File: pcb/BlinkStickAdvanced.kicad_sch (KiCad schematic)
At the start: 27 parts, among them J1 POWER, J2 USB_B_Micro, J3 ADD_HEADER_B, J4 ADD_HEADER_G, J5 ADD_HEADER_R, J6 RGB_HEADER, J7 RGB_HEADER, Q1 IRLR8726, Q2 IRLR8726, Q3 IRLR8726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

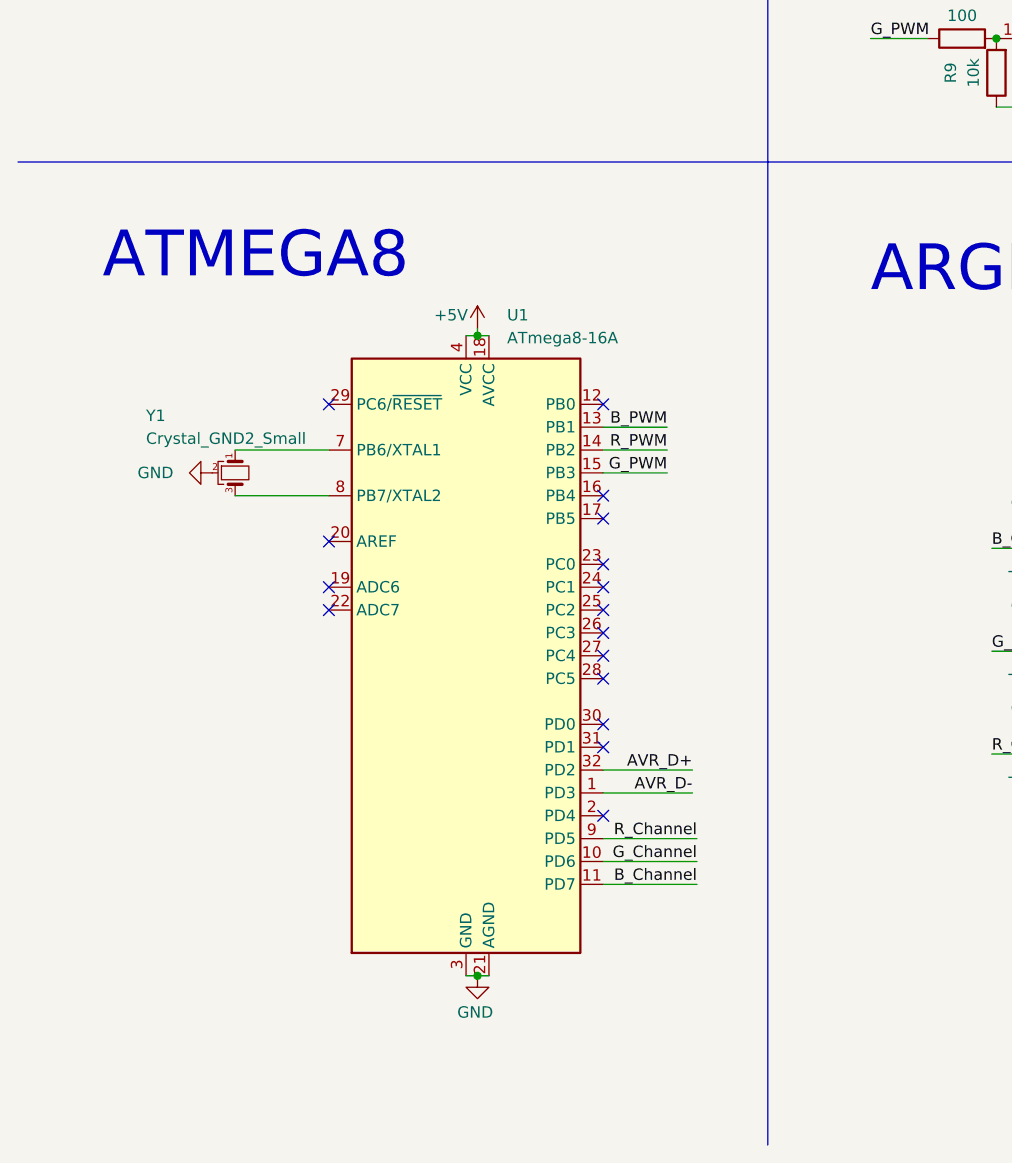
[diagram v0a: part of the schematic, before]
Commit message: USBaspLoader support for PCB.
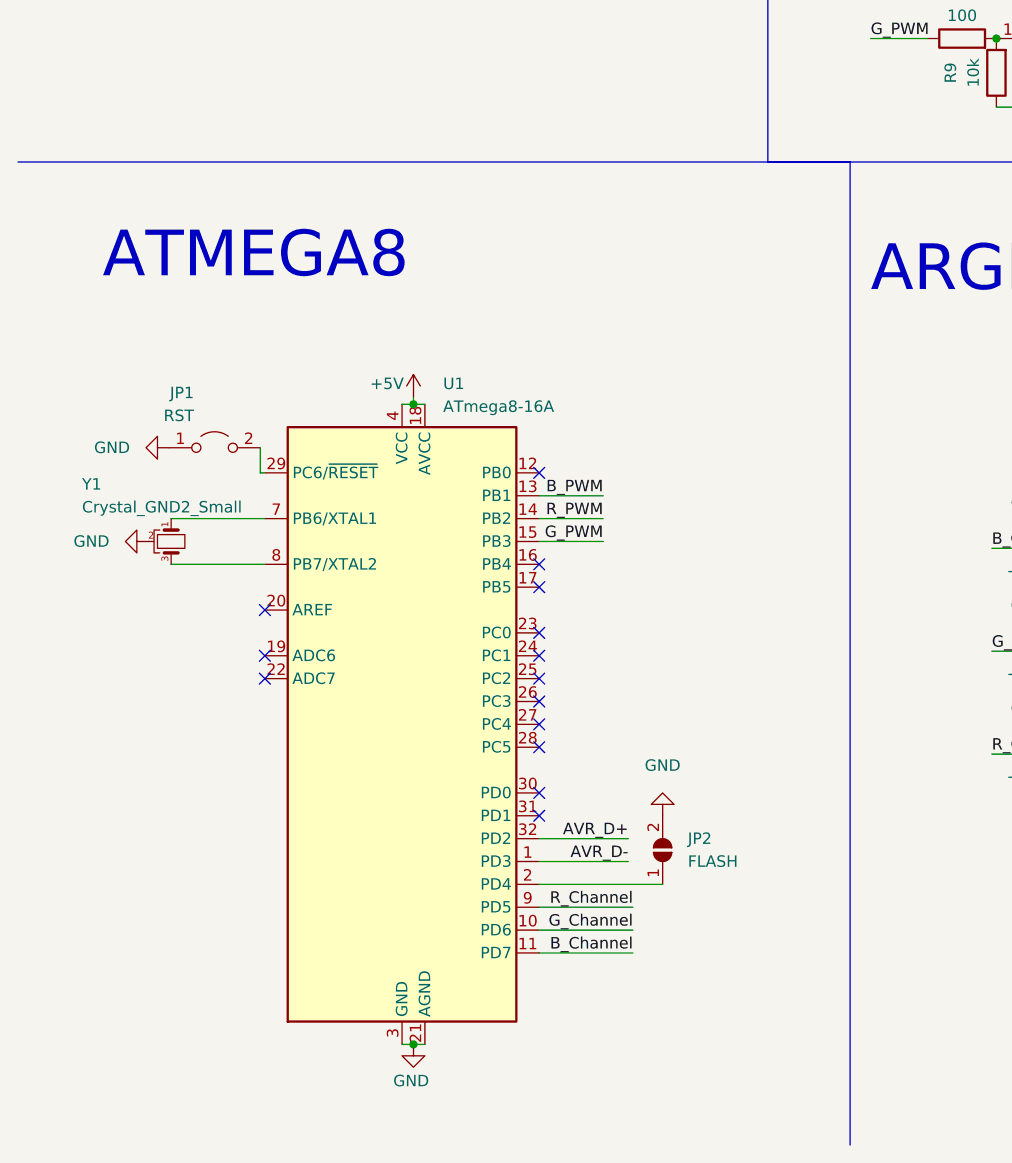
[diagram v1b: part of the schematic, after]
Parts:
- added JP1: RST, symbol Jumper:Jumper_2_Open
- added JP2: FLASH, symbol Jumper:SolderJumper_2_Open
- J1: footprint Connector_PinSocket_2.54mm:PinSocket_1x04_P2.54mm_Vertical -> TerminalBlock_Phoenix:TerminalBlock_Phoenix_MPT-0,5-4-2.54_1x04_P2.54mm_Horizontal
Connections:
- net GND: now also JP1.1 (A), JP2.2 (B)
- net at U1.2 (PD4): now also JP2.1 (A)
- net at U1.29 (PC6/~{RESET}): now also JP1.2 (B)
- no-connect marks 20 -> 18
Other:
- moved on the sheet: U1, Y1
